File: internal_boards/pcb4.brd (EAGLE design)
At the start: 100 x 80 mm, 9 parts, among them J1 22-27-2021-02, J2 22-27-2021-02

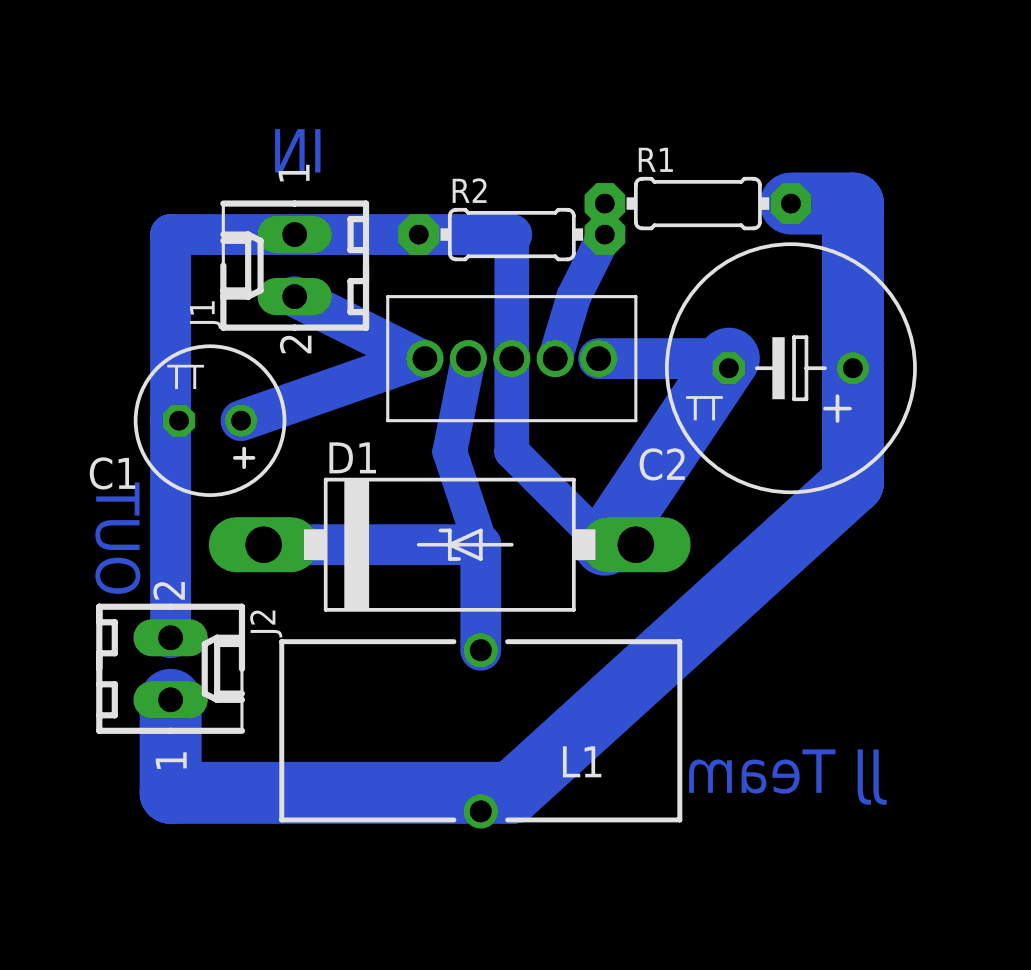
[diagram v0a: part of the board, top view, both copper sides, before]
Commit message: * Enhancement to board to use regulator with pins slightly spaced out
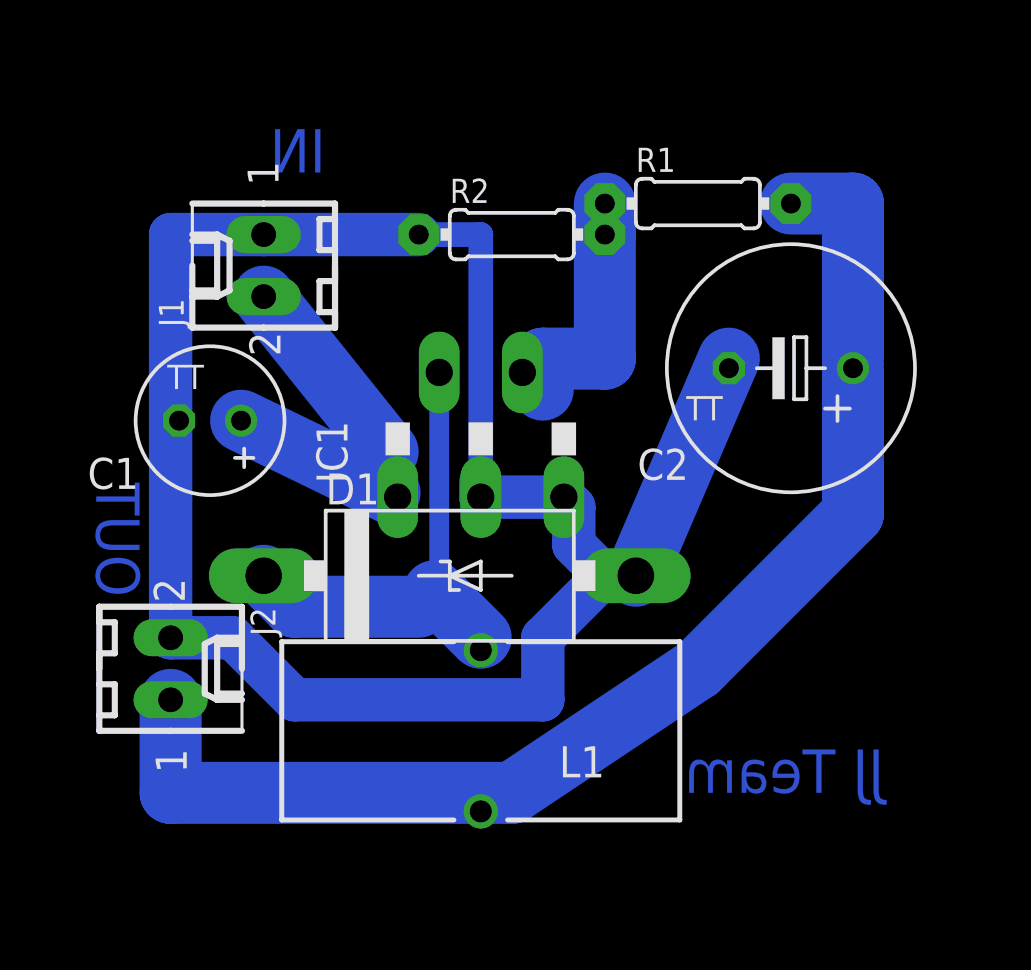
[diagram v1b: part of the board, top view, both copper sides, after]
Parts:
- removed U$1: LM2576, LM2576:LM2576
- added IC1: LM2576T-5.0, LM2576:TO220-5
- moved D1 1.27 mm to (49.5, 48.3)
- moved J1 1.27 mm to (41.9, 61.0)
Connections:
- net GND: now also IC1.3, IC1.5; no longer U$1.3, U$1.5
- net N$1: now also IC1.4; no longer U$1.4
- net N$2: now also IC1.1; no longer U$1.1
- net N$3: now also IC1.2; no longer U$1.2
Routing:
- net GND: track 61.3 -> 81.4 mm
- net N$2: track 13.6 -> 18.3 mm
- net N$1: track 6.76 -> 10.2 mm
- net N$3: track 21.1 -> 20.0 mm
- net N$4: track 52.1 -> 52.6 mm
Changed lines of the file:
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@@
 <?xml version="1.0" encoding="utf-8"?>
 <!DOCTYPE eagle SYSTEM "eagle.dtd">
-<eagle version="6.5.0">
+<eagle version="7.1.0">
 <drawing>
 <settings>
@@
 <pass name="Default">
 <param name="RoutingGrid" value="50mil"/>
+<param name="AutoGrid" value="1"/>
+<param name="Efforts" value="0"/>
+<param name="TopRouterVariant" value="1"/>
 <param name="tpViaShape" value="round"/>
 <param name="PrefDir.1" value="0"/>
@@
 </autorouter>
 <elements>
-<element name="U$1" library="LM2576" package="LM2576" value="LM2576" x="52.07" y="57.15"/>
-<element name="D1" library="diode" package="C4111-15" value="1N5908" x="49.53" y="49.53"/>
+<element name="D1" library="diode" package="C4111-15" value="1N5908" x="49.53" y="48.26"/>
 <element name="L1" library="resistor" package="TJ3-U1" value="" x="50.8" y="41.91" rot="R90"/>
 <element name="R1" library="adafruit" package="0204/7" value="" x="59.69" y="63.5"/>
 <element name="R2" library="adafruit" package="0204/7" value="" x="52.07" y="62.23"/>
-<element name="J1" library="con-molex" package="6410-02" value="22-27-2021-02" x="43.18" y="60.96" rot="R90">
-<attribute name="OC_NEWARK" value="unknown" x="49.53" y="88.9" size="1.778" layer="27" rot="R90" display="off"/>
-<attribute name="MPN" value="" x="49.53" y="88.9" size="1.778" layer="27" rot="R90" display="off"/>
-<attribute name="MF" value="" x="49.53" y="88.9" size="1.778" layer="27" rot="R90" display="off"/>
-<attribute name="OC_FARNELL" value="unknown" x="49.53" y="88.9" size="1.778" layer="27" rot="R90" display="off"/>
+<element name="J1" library="con-molex" package="6410-02" value="22-27-2021-02" x="41.91" y="60.96" rot="R90">
+<attribute name="OC_NEWARK" value="unknown" x="48.26" y="88.9" size="1.778" layer="27" rot="R90" display="off"/>
+<attribute name="MPN" value="" x="48.26" y="88.9" size="1.778" layer="27" rot="R90" display="off"/>
+<attribute name="MF" value="" x="48.26" y="88.9" size="1.778" layer="27" rot="R90" display="off"/>
+<attribute name="OC_FARNELL" value="unknown" x="48.26" y="88.9" size="1.778" layer="27" rot="R90" display="off"/>
 </element>
 <element name="J2" library="con-molex" package="6410-02" value="22-27-2021-02" x="38.1" y="44.45" rot="R270">
@@
 <element name="C2" library="adafruit" package="TT5D10" value="" x="63.5" y="56.75715" rot="R180"/>
 <element name="C1" library="adafruit" package="TT2D6" value="" x="39.71484375" y="54.61" rot="R180"/>
+<element name="IC1" library="LM2576" package="TO220-5" value="LM2576T-5.0" x="50.8" y="59.69"/>
 </elements>
 <signals>
 <signal name="GND">
-<contactref element="U$1" pad="5"/>
-<contactref element="U$1" pad="3"/>
 <contactref element="D1" pad="A"/>
 <contactref element="R2" pad="1"/>
 <contactref element="J1" pad="1"/>
 <contactref element="J2" pad="2"/>
-<wire x1="55.88" y1="49.53" x2="60.96" y2="57.15" width="2.54" layer="16"/>
-<wire x1="57.15" y1="49.53" x2="55.88" y2="49.53" width="1.016" layer="16"/>
-<wire x1="48.26" y1="62.23" x2="43.18" y2="62.23" width="1.6764" layer="16"/>
-<wire x1="52.07" y1="62.23" x2="52.07" y2="57.15" width="1.4224" layer="16"/>
-<wire x1="48.26" y1="62.23" x2="52.07" y2="62.23" width="1.6764" layer="16"/>
-<wire x1="52.07" y1="53.34" x2="55.88" y2="49.53" width="1.4224" layer="16"/>
-<wire x1="52.07" y1="57.15" x2="52.07" y2="53.34" width="1.4224" layer="16"/>
+<wire x1="57.15" y1="48.26" x2="60.96" y2="57.15" width="2.54" layer="16"/>
+<wire x1="48.26" y1="62.23" x2="41.91" y2="62.23" width="1.778" layer="16"/>
 <contactref element="C2" pad="-"/>
 <contactref element="C1" pad="-"/>
-<wire x1="55.626" y1="57.15" x2="60.96" y2="57.15" width="1.6764" layer="16"/>
 <wire x1="60.96" y1="57.15" x2="60.96" y2="56.75715" width="0.254" layer="16"/>
-<wire x1="38.1" y1="45.72" x2="38.1" y2="54.61" width="1.6764" layer="16"/>
-<wire x1="38.1" y1="62.23" x2="38.1" y2="54.61" width="1.6764" layer="16"/>
-<wire x1="43.18" y1="62.23" x2="38.1" y2="62.23" width="1.6764" layer="16"/>
+<wire x1="38.1" y1="45.72" x2="38.1" y2="54.61" width="1.778" layer="16"/>
+<wire x1="38.1" y1="62.23" x2="38.1" y2="54.61" width="1.778" layer="16"/>
+<wire x1="41.91" y1="62.23" x2="38.1" y2="62.23" width="1.778" layer="16"/>
 <wire x1="38.1" y1="54.61" x2="38.44484375" y2="54.61" width="0.254" layer="16"/>
+<contactref element="IC1" pad="3"/>
+<contactref element="IC1" pad="5"/>
+<wire x1="57.15" y1="48.26" x2="55.88" y2="48.26" width="1.778" layer="16"/>
+<wire x1="55.88" y1="48.26" x2="54.61" y2="49.53" width="1.778" layer="16"/>
+<wire x1="54.61" y1="49.53" x2="54.61" y2="51.0728" width="1.778" layer="16"/>
+<wire x1="54.61" y1="51.0728" x2="54.2036" y2="51.4792" width="1.778" layer="16"/>
+<wire x1="50.8" y1="51.4792" x2="50.8" y2="52.07" width="1.778" layer="16"/>
+<wire x1="50.8" y1="51.4792" x2="54.2036" y2="51.4792" width="1.778" layer="16"/>
+<wire x1="48.26" y1="62.23" x2="50.8" y2="62.23" width="1.016" layer="16"/>
+<wire x1="50.8" y1="62.23" x2="50.8" y2="52.07" width="1.016" layer="16"/>
+<wire x1="38.1" y1="45.72" x2="40.64" y2="45.72" width="1.778" layer="16"/>
+<wire x1="40.64" y1="45.72" x2="43.18" y2="43.18" width="1.778" layer="16"/>
+<wire x1="43.18" y1="43.18" x2="53.34" y2="43.18" width="1.778" layer="16"/>
+<wire x1="53.34" y1="43.18" x2="53.34" y2="45.72" width="1.778" layer="16"/>
+<wire x1="53.34" y1="45.72" x2="55.88" y2="48.26" width="1.778" layer="16"/>
 </signal>
 <signal name="N$2">
-<contactref element="U$1" pad="1"/>
 <contactref element="J1" pad="2"/>
-<wire x1="48.514" y1="57.15" x2="48.26" y2="57.15" width="0.254" layer="16"/>
-<wire x1="48.26" y1="57.15" x2="43.18" y2="59.69" width="1.6764" layer="16"/>
+<wire x1="46.99" y1="53.34" x2="41.91" y2="59.69" width="2.54" layer="16"/>
 <contactref element="C1" pad="+"/>
-<wire x1="48.26" y1="57.15" x2="40.98484375" y2="54.61" width="1.6764" layer="16"/>
-</signal>
-<signal name="N$3">
-<contactref element="U$1" pad="2"/>
-<contactref element="D1" pad="C"/>
-<contactref element="L1" pad="2"/>
-<wire x1="41.91" y1="49.53" x2="50.8" y2="49.53" width="1.6764" layer="16"/>
-<wire x1="50.8" y1="49.53" x2="50.8" y2="45.21" width="1.6764" layer="16"/>
-<wire x1="50.8" y1="49.53" x2="49.53" y2="53.34" width="1.4224" layer="16"/>
-<wire x1="49.53" y1="53.34" x2="50.292" y2="57.15" width="1.4224" layer="16"/>
+<wire x1="46.99" y1="53.34" x2="47.066609375" y2="51.653346875" width="1.6764" layer="16"/>
+<contactref element="IC1" pad="1"/>
+<wire x1="47.066609375" y1="51.653346875" x2="40.98484375" y2="54.61" width="2.54" layer="16"/>
+<wire x1="47.3202" y1="50.927" x2="47.3202" y2="51.6636" width="0.254" layer="16"/>
+<wire x1="47.3202" y1="51.6636" x2="47.3964" y2="51.4792" width="0.254" layer="16"/>
+<wire x1="47.3202" y1="50.927" x2="47.066609375" y2="51.653346875" width="0.254" layer="16"/>
 </signal>
 <signal name="N$4">
@@
 <wire x1="66.04" y1="63.5" x2="66.04" y2="57.15" width="2.54" layer="16"/>
 <wire x1="63.5" y1="63.5" x2="66.04" y2="63.5" width="2.54" layer="16"/>
-<wire x1="66.04" y1="52.07" x2="52.07" y2="39.37" width="2.54" layer="16"/>
-<wire x1="66.04" y1="56.75715" x2="66.04" y2="52.07" width="2.54" layer="16"/>
+<wire x1="66.04" y1="50.8" x2="59.69" y2="44.45" width="2.54" layer="16"/>
+<wire x1="59.69" y1="44.45" x2="52.07" y2="39.37" width="2.54" layer="16"/>
+<wire x1="66.04" y1="56.75715" x2="66.04" y2="50.8" width="2.54" layer="16"/>
 <wire x1="52.07" y1="39.37" x2="50.8" y2="38.61" width="0.254" layer="16"/>
 <wire x1="66.04" y1="57.15" x2="66.04" y2="56.75715" width="0.254" layer="16"/>
@@
 <contactref element="R1" pad="1"/>
 <contactref element="R2" pad="2"/>
-<contactref element="U$1" pad="4"/>
-<wire x1="54.61" y1="59.69" x2="53.848" y2="57.15" width="1.4224" layer="16"/>
-<wire x1="55.88" y1="62.23" x2="55.88" y2="63.5" width="1.016" layer="16"/>
-<wire x1="55.88" y1="62.23" x2="54.61" y2="59.69" width="1.4224" layer="16"/>
+<wire x1="55.88" y1="62.23" x2="55.88" y2="63.5" width="2.54" layer="16"/>
+<contactref element="IC1" pad="4"/>
+<wire x1="55.88" y1="62.23" x2="55.88" y2="57.15" width="2.54" layer="16"/>
+<wire x1="55.88" y1="57.15" x2="53.34" y2="57.15" width="2.54" layer="16"/>
+<wire x1="53.34" y1="57.15" x2="53.34" y2="55.88" width="2.54" layer="16"/>
+<wire x1="53.34" y1="55.88" x2="52.5018" y2="56.5846" width="0" layer="19" extent="1-16"/>
+</signal>
+<signal name="N$3">
+<contactref element="D1" pad="C"/>
+<contactref element="IC1" pad="2"/>
+<contactref element="L1" pad="2"/>
+<wire x1="49.0982" y1="56.5846" x2="49.0982" y2="47.8282" width="0.8128" layer="16"/>
+<wire x1="49.0982" y1="47.8282" x2="48.895" y2="47.625" width="0.8128" layer="16"/>
+<wire x1="48.895" y1="47.625" x2="48.26" y2="46.99" width="0.8128" layer="16"/>
+<wire x1="48.26" y1="46.99" x2="43.18" y2="46.99" width="2.54" layer="16"/>
+<wire x1="43.18" y1="46.99" x2="41.91" y2="48.26" width="2.54" layer="16"/>
+<wire x1="50.8" y1="45.21" x2="50.8" y2="45.72" width="0.8128" layer="16"/>
+<wire x1="50.8" y1="45.72" x2="48.895" y2="47.625" width="2.54" layer="16"/>
 </signal>
 </signals>

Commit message: * Setting values of components in Schematic.
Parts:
- C1: value (none) -> 100uF (16V)
- C2: value (none) -> 330uF (16V)
- D1: value 1N5908 -> 1N5822
- L1: value (none) -> 100uH (3amp)
- R1: value (none) -> 4.7k
- R2: value (none) -> 1.5k
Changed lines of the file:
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@@
 </autorouter>
 <elements>
-<element name="D1" library="diode" package="C4111-15" value="1N5908" x="49.53" y="48.26"/>
-<element name="L1" library="resistor" package="TJ3-U1" value="" x="50.8" y="41.91" rot="R90"/>
-<element name="R1" library="adafruit" package="0204/7" value="" x="59.69" y="63.5"/>
-<element name="R2" library="adafruit" package="0204/7" value="" x="52.07" y="62.23"/>
+<element name="D1" library="diode" package="C4111-15" value="1N5822" x="49.53" y="48.26"/>
+<element name="L1" library="resistor" package="TJ3-U1" value="100uH (3amp)" x="50.8" y="41.91" rot="R90"/>
+<element name="R1" library="adafruit" package="0204/7" value="4.7k" x="59.69" y="63.5"/>
+<element name="R2" library="adafruit" package="0204/7" value="1.5k" x="52.07" y="62.23"/>
 <element name="J1" library="con-molex" package="6410-02" value="22-27-2021-02" x="41.91" y="60.96" rot="R90">
 <attribute name="OC_NEWARK" value="unknown" x="48.26" y="88.9" size="1.778" layer="27" rot="R90" display="off"/>
@@
 <attribute name="OC_FARNELL" value="unknown" x="15.24" y="25.4" size="1.778" layer="27" rot="R270" display="off"/>
 </element>
-<element name="C2" library="adafruit" package="TT5D10" value="" x="63.5" y="56.75715" rot="R180"/>
-<element name="C1" library="adafruit" package="TT2D6" value="" x="39.71484375" y="54.61" rot="R180"/>
+<element name="C2" library="adafruit" package="TT5D10" value="330uF (16V)" x="63.5" y="56.75715" rot="R180"/>
+<element name="C1" library="adafruit" package="TT2D6" value="100uF (16V)" x="39.71484375" y="54.61" rot="R180"/>
 <element name="IC1" library="LM2576" package="TO220-5" value="LM2576T-5.0" x="50.8" y="59.69"/>
 </elements>
